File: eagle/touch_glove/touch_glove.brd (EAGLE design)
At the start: 160 x 100 mm, 139 parts, among them P1 PELTIER, P2 PELTIER, P3 PELTIER, P4 PELTIER, P5 PELTIER, U1 DRV8837C, U2 DRV8837C, U3 DRV8837C, U4 DRV8837C, U5 DRV8837C, U6 ATMEGA128RFA1, Y1 16MHz

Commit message: Changed power symbols for Glove
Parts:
- added BATT1: BATTERYPTH_HOLES, MrSwirlyEyes:DUAL_PTH_PADS
- added C63, C64, C65, C66, C69, C70, C71: 10uF/25V, MrSwirlyEyes:CAP_CER_SMD-805
- added C67: 220uF/16V, MrSwirlyEyes:CAP_POL_SMD_L6.6-W6.6
- added C68, C74, C75, C76: 0.1uF/50V, MrSwirlyEyes:CAP_CER_SMD-805
- added C78: 100UF/16V, MrSwirlyEyes:CAP_POL_SMD_L6.6-W6.6
- added C79: 1uF/25V, MrSwirlyEyes:CAP_CER_SMD-805
- added D6, D7, D8: 1A/50V, MrSwirlyEyes:DIODE_SMD_1A-50V-SOD123F
- added L1, L2: 10uH, MrSwirlyEyes:INDUCTOR_SMD-805
- added SW1: 5A/28V, MrSwirlyEyes:SW-SLIDE_SPDT_5A-28V_13L-7W
- added U$1, U$2: NET_BRIDGE, MrSwirlyEyes:NET_BRIDGE
- added VREG1, VREG2: 1.5A/3.3V, MrSwirlyEyes:SOT223-4
- added VREG3: 1.5A/2.5V, MrSwirlyEyes:SOT223-4
- R1, R10, R11, R12, R13, R14, R15, R16, R17, R18, R19, R2, R20, R21, R22, R23, R24, R25, R26, R27, R28, R29, R3, R30, R31, R32, R33, R34, R35, R36, R37, R38, R4, R5, R6, R7, R8, R9: device MrSwirlyEyes:RESC2012X60_HS -> MrSwirlyEyes:RESISTOR_SMD-805
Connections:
- new net 3.3V: C65.1, C70.1, D7.A, D8.A, VREG2.3, VREG3.3
- new net N$38: L2.2, U$2.P$1
- new net N$40: C64.1, C66.1, C67.A, C68.1, C69.1, C71.1, C78.A, D6.K, D7.K, D8.K, SW1.P$1, VREG1.1, VREG2.1, VREG3.1
- new net N$43: BATT1.+, SW1.P$2
- new net NGND: C79.2, U$1.P$1, U$2.P$2
- net GND: now also BATT1.-, C63.2, C64.2, C65.2, C66.2, C67.K, C68.2, C69.2, C70.2, C71.2, C74.2, C78.K, L2.1, U$1.P$2, VREG1.2, VREG1.4, VREG2.2, VREG2.4, VREG3.2, VREG3.4
- net VCC: now also C63.1, C74.1, C79.1, D6.A, L1.1, L1.2, VREG1.3

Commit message: Unity to RED board test added.  Unity to Arduino test moved.  Several changes to Touch Glove sch and brd
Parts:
- removed C76: 0.1uF/50V, MrSwirlyEyes:CAP_CER_SMD-805
- removed D8: 1A/50V, MrSwirlyEyes:DIODE_SMD_1A-50V-SOD123F
- removed VREG1: 1.5A/3.3V, MrSwirlyEyes:SOT223-4
- added C72, C77: 10uF/25V, MrSwirlyEyes:CAP_CER_SMD-805
- added C73, C80: 0.1uF/50V, MrSwirlyEyes:CAP_CER_SMD-805
- added C81: 100UF/16V, MrSwirlyEyes:CAP_POL_SMD_L6.6-W6.6
- added C82: 220uF/16V, MrSwirlyEyes:CAP_POL_SMD_L6.6-W6.6
- added D9: 1A/50V, MrSwirlyEyes:DIODE_SMD_1A-50V-SOD123F
- added VREG4: 3A/2.5V, MrSwirlyEyes:DDPAK-5
- C64, C66, C70: value 10uF/25V -> 0.1uF/50V
- C74: value 0.1uF/50V -> 10uF/25V
- VREG3: value 1.5A/2.5V -> 1A/3.3V; device MrSwirlyEyes:SOT223-4 -> MrSwirlyEyes:SOIC-8_W3.9MM
- moved C71 1313.3 mm to (-345.4, -1162.0)
- moved C70 1305.6 mm to (-335.3, -1162.0)
- moved VREG3 1305.5 mm to (-356.9, -1168.4)
- moved C66 1289.9 mm to (-360.7, -1162.0)
- moved C65 1281.2 mm to (-340.4, -1162.0)
- moved C64 121.8 mm to (-350.5, -1162.0)
- moved C63 108.8 mm to (-330.2, -1162.0)
- moved C74 96.6 mm to (-355.6, -1162.0)
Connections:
- net 3.3V: now also C75.1, C77.1, C80.1, C81.A, C82.A, D9.A, VREG4.4, VREG4.5; no longer C70.1, D8.A, VREG3.3
- net GND: now also C72.2, C73.2, C75.2, C77.2, C80.2, C81.K, C82.K, VREG3.1, VREG4.3, VREG4.TAB; no longer VREG1.2, VREG1.4, VREG3.4
- net N$40: now also C72.1, C73.1, C74.1, D9.K, VREG3.3, VREG3.4, VREG4.1, VREG4.2; no longer D8.K, VREG1.1, VREG3.1
- net VCC: now also C70.1, VREG3.5, VREG3.6; no longer C74.1, VREG1.3

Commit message: Rev 1 of Touch Glove schematic complete.  Putting Touch Glove PCB on hold until Robotic Arm schematic + PCB are done
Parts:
- moved VREG4 1226.4 mm to (68.5, 40.6)
- moved BATT1 1165.6 mm to (-128.3, 102.9)
- moved C62 1165.6 mm to (-138.4, 137.2)
- moved C81 1165.6 mm to (-245.1, 10.2)
- moved JP1 1165.6 mm to (-130.8, 123.2)
- moved SW1 1165.6 mm to (-120.7, 74.9)
- moved U$1 1165.6 mm to (-139.7, 91.4)
- moved VREG3 1165.6 mm to (-283.2, -5.08)
- moved C63 1165.6 mm to (-256.5, 1.27)
- moved C64 1165.6 mm to (-276.9, 1.27)
- moved C65 1165.6 mm to (-266.7, 1.27)
- moved C66 1165.6 mm to (-287.0, 1.27)
- moved C67 1165.6 mm to (-166.4, 52.1)
- moved C68 1165.6 mm to (-182.9, 48.3)
- moved C69 1165.6 mm to (-188.0, 48.3)
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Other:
- board size 160 x 100 mm -> 88.9 x 50.8 mm
- board text removed: "initializing touch_glove"

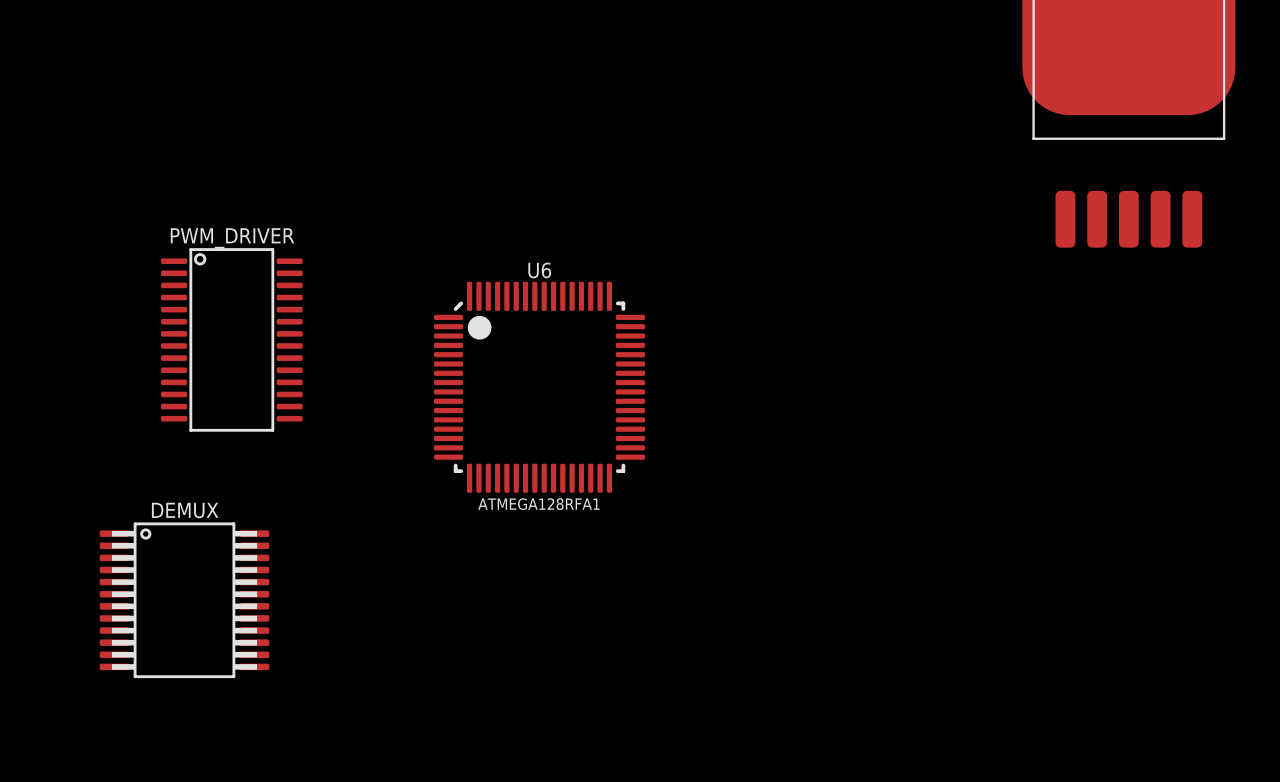
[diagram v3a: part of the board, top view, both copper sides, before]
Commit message: Replaced 2.5V regulator for TECs to 1.8V regulator for TECs.  2.5V got way too hot.  But 1.8V can be used effectively
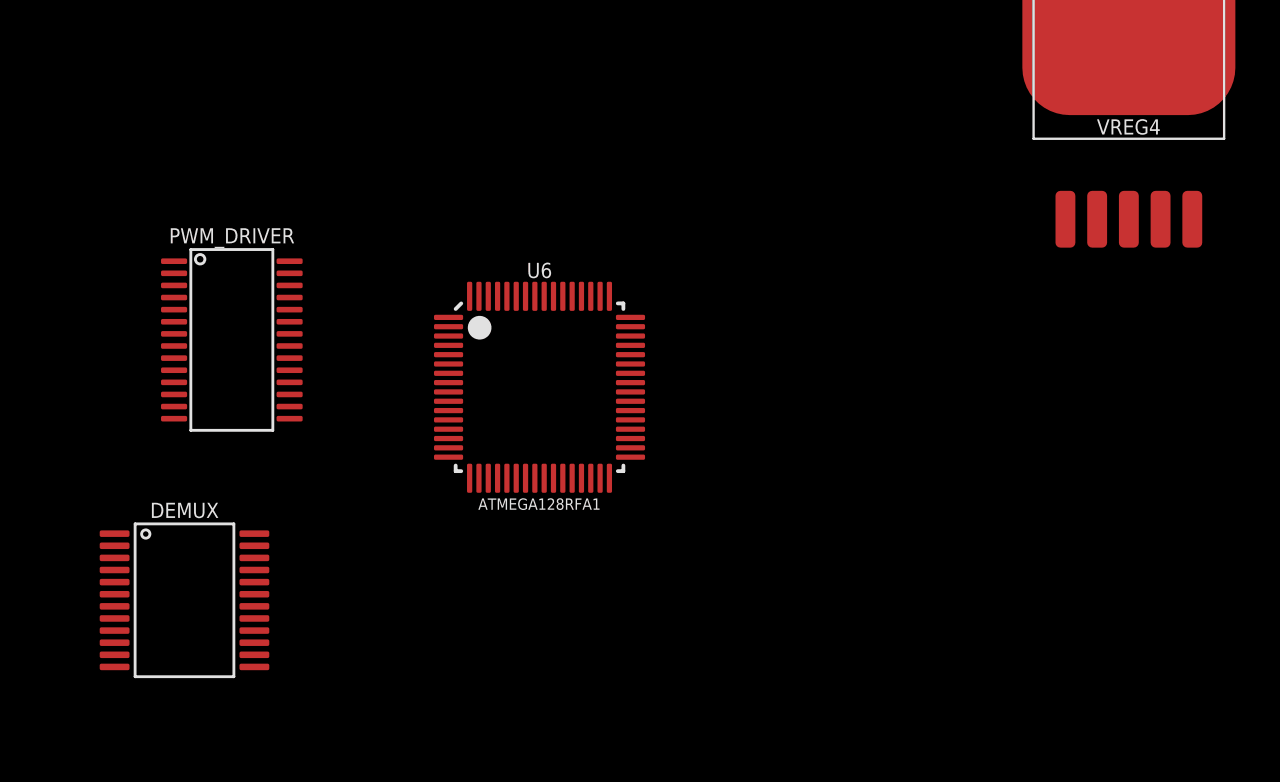
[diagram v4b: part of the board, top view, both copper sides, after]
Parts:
- J1: value (none) -> AVR ISP
- VREG4: value 3A/2.5V -> 3A/1.8V
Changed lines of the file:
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@@
 <attribute name="TESTED" value="NO" x="-173.99" y="-73.66" size="1.778" layer="27" display="off"/>
 </element>
-<element name="J1" library="MrSwirlyEyes" package="2X3-NS" value="" x="-123.19" y="144.78">
+<element name="J1" library="MrSwirlyEyes" package="2X3-NS" value="AVR ISP" x="-123.19" y="144.78">
 <attribute name="DATASHEET" value="http://portal.fciconnect.com/Comergent//fci/drawing/67996.pdf" x="-123.19" y="144.78" size="1.778" layer="27" display="off"/>
 <attribute name="DIST" value="Digikey" x="-123.19" y="144.78" size="1.778" layer="27" display="off"/>
@@
 <attribute name="MFR" value="Amphenol FCI" x="-123.19" y="144.78" size="1.778" layer="27" display="off"/>
 <attribute name="MPN" value="67997-206HLF" x="-123.19" y="144.78" size="1.778" layer="27" display="off"/>
+<attribute name="VALUE" value="AVR ISP" x="-123.19" y="144.78" size="1.778" layer="27" display="off"/>
 </element>
 <element name="C62" library="MrSwirlyEyes" package="CAP_CER_SMD-805" value="0.1uF/50V" x="-138.43" y="137.16">
@@
 <attribute name="TESTED" value="NO" x="-224.79" y="38.1" size="1.778" layer="27" display="off"/>
 </element>
-<element name="VREG4" library="MrSwirlyEyes" package="DDPAK-5" value="3A/2.5V" x="68.453" y="40.64">
+<element name="VREG4" library="MrSwirlyEyes" package="DDPAK-5" value="3A/1.8V" x="68.453" y="40.64">
 <attribute name="CREATOR" value="MrSwirlyEyes" x="68.453" y="40.64" size="1.778" layer="27" display="off"/>
 <attribute name="DATASHEET" value="http://cds.linear.com/docs/en/datasheet/1764fb.pdf" x="68.453" y="40.64" size="1.778" layer="27" display="off"/>
 <attribute name="DIST" value="Digikey" x="68.453" y="40.64" size="1.778" layer="27" display="off"/>
-<attribute name="DISTLINK" value="https://www.digikey.com/products/en?keywords=LT1764EQ-2.5%23PBF-ND" x="68.453" y="40.64" size="1.778" layer="27" display="off"/>
-<attribute name="DISTPN" value="LT1764EQ-2.5#PBF-ND" x="68.453" y="40.64" size="1.778" layer="27" display="off"/>
+<attribute name="DISTLINK" value="https://www.digikey.com/products/en?keywords=LT1764EQ-1.8%23PBF" x="68.453" y="40.64" size="1.778" layer="27" display="off"/>
+<attribute name="DISTPN" value="LT1764EQ-1.8#PBF-ND" x="68.453" y="40.64" size="1.778" layer="27" display="off"/>
 <attribute name="MFR" value="Linear Technology" x="68.453" y="40.64" size="1.778" layer="27" display="off"/>
-<attribute name="MPN" value="LT1764EQ-2.5#PBF" x="68.453" y="40.64" size="1.778" layer="27" display="off"/>
+<attribute name="MPN" value="LT1764EQ-1.8#PBF" x="68.453" y="40.64" size="1.778" layer="27" display="off"/>
 </element>
 <element name="C72" library="MrSwirlyEyes" package="CAP_CER_SMD-805" value="10uF/25V" x="-229.87" y="17.78">

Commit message: Modified code to work with new PCB board.  Removed libraries, placed in new repo.  Finished and printed Robotic Arm PCB board.  Tested and WORKS!  Started on Touch Glove PCB
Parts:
- removed A1: ANTENNASMD5, lib_kenmei:ANTENNA-CHIP5
- removed B1: 748421245, lib_kenmei:0805_BALUN
- removed C36, C38, C40, C41, C47: 1uF/25V, MrSwirlyEyes:CAP_CER_SMD-805
- removed C37, C39, C46, C51, C62: 0.1uF/50V, MrSwirlyEyes:CAP_CER_SMD-805
- removed C42, C43: 12pF/250V, MrSwirlyEyes:CAP_CER_SMD-805
- removed C44: 22PF/250V, MrSwirlyEyes:CAP_CER_SMD-805
- removed C45: 0.75PF/100V, MrSwirlyEyes:CAP_CER_SMD-805
- removed C48: 0.22uF/50V, MrSwirlyEyes:CAP_CER_SMD-805
- removed C49, C50: 10uF/25V, MrSwirlyEyes:CAP_CER_SMD-805
- removed DEMUX: CH16_MUX-DEMUX, MrSwirlyEyes:SSOP-24
- removed IMU1: LM9DS1, lib_kenmei:LSM9DS1_LGA24L
- removed J1: AVR ISP, MrSwirlyEyes:2X3-NS
- removed JP1: FTDIPTH-RA, MrSwirlyEyes:FTDI_BASIC-6PIN-MALE-RA
- removed R38: 10KΩ, MrSwirlyEyes:RESISTOR_SMD-805
- removed U6: ATMEGA128RFA1, MrSwirlyEyes:VFQFN-64
- removed Y1: 16MHz, MrSwirlyEyes:CRYSTAL-SMD-5X3
- added A6: 2.4GHz/802.11/0.5dBi/3W, PiB_radio_frequency:ANTENNA-CHIP5
- added ANALOG_BR, NOISE_BR: 2PT_GND_TIE, PiB_power_symbols:2PT_GND_TIE
- added AVR_ISP: AVR ISP, PiB_connectors:2X3-NS
- added B2: Impedence UNBAL/BAL (50Ω/100Ω), PiB_radio_frequency:0805_BALUN
- added BATT2: BATTERYPTH_HOLES, PiB:DUAL_PTH_PADS
- added C100, C106, C108, C116, C117, C119, C121, C122, C124, C127, C129, C135, C98: 0.1uF/50V, PiB_capacitors:_CER_SMD-805
- added C107, C109, C110, C111, C132, C134, C136: 1uF/25V, PiB_capacitors:_CER_SMD-805
- added C112, C113: 12pF/250V, PiB_capacitors:_CER_SMD-805
- added C114: 22PF/250V, PiB_capacitors:_CER_SMD-805
- added C115: 0.75PF/100V, PiB_capacitors:_CER_SMD-805
- added C118: 220uF/16V, PiB_capacitors:_AE_SMD_L6.6-W6.6
- added C120, C123, C125, C126, C128, C97, C99: 10uF/25V, PiB_capacitors:_CER_SMD-805
- added C133: 100UF/16V, PiB_capacitors:_AE_SMD_L6.6-W6.6
- added D10, D11, D8: 1A/50V, PiB_discrete_semiconductors:SOD123F
- added D12: 1A/50V, MrSwirlyEyes:DIODE_SMD_1A-50V-SOD123F
- added DEMUX1: CH16_MUX-DEMUX, PiB:SSOP-24
- added J2: (ID,OD)=(2.1,5.5)MM, PiB_connectors:POWER_JACK_SLOT_ID2.1MM-OD5.5MM
- added JP2: FTDIPTH-RA, PiB_connectors:FTDI_BASIC-6PIN-MALE-RA
- added L3, L4: 10uH, PiB_inductors:_SMD-805
- added L5: BLUE, PiB_leds:LED_SMD-805_
- added L6: GREEN, PiB_leds:LED_SMD-805_
- added L7: RED, PiB_leds:LED_SMD-805_
- added MCU: ATMEGA128RFA1, PiB_ic_microcontrollers:VFQFN-64
- added PWM_DRIVER1: PCA9685, PiB:TSSOP-28
- added R40, R41: 4.7K, PiB_resistors:RESISTOR_SMD-805
- added R46, R47: 10KΩ, PiB_resistors:RESISTOR_SMD-805
- added R48: 2KΩ, PiB_resistors:RESISTOR_SMD-805
- added R49: 1KΩ, PiB_resistors:RESISTOR_SMD-805
- added S7: TACTILE-SW_500mA/12V, PiB_switches:BTN_MOMENTARY_SPST-NO_SMD_12V_50MA_L5.2-W5.2
- added SW2: 5A/28V, PiB_switches:SW_TOGGLE_SPDT_5A-28V_13L-7W
- added VIBE_6: VIBE_MOTOR, MrSwirlyEyes:CONNECTOR_VIBE-MOTOR
- added VIBE_T6: 2.6A/20V/57mΩ, MrSwirlyEyes:SOT23-3
- added VREG1: 1A/3.3V, PiB_ic_power:SOIC-8_W3.9MM
- added VREG5: 5A/5V, PiB_ic_power:TO-263-5
- added Y2: 16MHz, PiB:CRYSTAL-SMD-5X3
- C1: value 10uF/25V -> 0.1uF/50V
- C35: value 0.1uF/50V -> 10uF/25V
- R12: value 4.7K -> 10KΩ
- R13: value 4.7K -> 100Ω
- moved R12 399.9 mm to (-276.9, -266.7)
- moved R13 395.9 mm to (-271.8, -266.7)
- moved C24 393.5 mm to (-287.0, -266.7)
- moved C1 357.5 mm to (-266.7, -259.1)
- moved C35 331.6 mm to (-281.9, -266.7)
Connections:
- removed net C5: DEMUX.4
- removed net C6: DEMUX.3
- removed net C7: DEMUX.2
- removed net C8: DEMUX.23
- removed net C9: DEMUX.22
- removed net N$33: B1.4, U6.8
- removed net N$34: B1.2, C44.1
- removed net N$35: C42.1, U6.56, Y1.1
- removed net N$36: C49.1, IMU1.21
- removed net N$37: C48.1, IMU1.24
- removed net N$39: A1.FEED, B1.1, C45.1
- removed net N$41: C62.1, JP1.DTR
- removed net N$42: JP1.CTS
- removed net S0: DEMUX.10
- removed net S1: DEMUX.11
- removed net S2: DEMUX.14
- removed net S3: DEMUX.13
- removed net SIG: DEMUX.1
- new net 5V: C121.1, C125.1, C133.A, D10.A, VREG5.4
- new net AGND: ANALOG_BR.P$2, C100.2, C122.2, C134.2, C135.2, C136.2, C97.2, DEMUX1.12, DEMUX1.15, MCU.58, MCU.61
- new net AVCC: C100.1, C122.1, C134.1, C135.1, C136.1, C97.1, DEMUX1.24, L3.2, MCU.59, MCU.62
- new net BATT_+: BATT2.+, J2.PWR, SW2.2
- new net BATT_-: BATT2.-, J2.GND@2
- new net N$44: C113.1, MCU.57, Y2.3
- new net N$45: B2.3, MCU.9
- new net N$46: B2.4, MCU.8
- new net N$47: B2.2, C114.1
- new net N$48: C112.1, MCU.56, Y2.1
- new net N$49: A6.FEED, B2.1, C115.1
- new net N$50: C117.1, JP2.DTR
- new net N$51: JP2.CTS
- new net N$52: ANALOG_BR.P$1, L4.2
- new net N$53: L5.K, R47.2
- new net N$54: L6.K, R49.2
- new net N$55: L7.K, R48.2
- new net N$62: C132.1, MCU.21, MCU.22
- new net N$63: C110.1, MCU.60
- new net STRAIN_10: DEMUX1.22
- new net STRAIN_6: DEMUX1.4
- new net STRAIN_7: DEMUX1.3
- new net STRAIN_8: DEMUX1.2
- new net STRAIN_9: DEMUX1.23
- new net VBATT: C118.A, C119.1, C120.1, C126.1, C127.1, C128.1, C129.1, D10.K, D8.K, L5.A, SW2.1, VREG1.3, VREG1.4, VREG5.1, VREG5.2
- new net VIBE_6: PWM_DRIVER.22, R12.2, R13.1
- net A0: now also MCU.63; no longer U6.63
- net A1: now also MCU.64; no longer U6.64
- net A2: now also MCU.1; no longer U6.1
- net A3: now also MCU.2; no longer U6.2
- net A4: now also MCU.3; no longer U6.3
- net A5: now also DEMUX1.1, MCU.4; no longer U6.4
- net A6: now also MCU.5; no longer U6.5
- net A7: now also MCU.6; no longer U6.6
- net C10: now also DEMUX1.21; no longer DEMUX.21
- net C11: now also DEMUX1.20; no longer DEMUX.20
- net C12: now also DEMUX1.19; no longer DEMUX.19
- net C13: now also DEMUX1.18; no longer DEMUX.18
- net C14: now also DEMUX1.17; no longer DEMUX.17
- net C15: now also DEMUX1.16; no longer DEMUX.16
- net GND: now also AVR_ISP.6, B2.5, C106.2, C107.2, C108.2, C109.2, C110.2, C111.2, C112.2, C113.2, C114.2, C115.2, C116.2, C118.K, C119.2, C120.2, C123.2, C124.2, C126.2, C127.2, C132.2, C98.2, C99.2, J2.GND@1, JP2.GND, L4.1, MCU.10, MCU.11, MCU.20, MCU.24, MCU.33, MCU.35, MCU.45, MCU.55, MCU.7, NOISE_BR.P$2, PWM_DRIVER1.1, PWM_DRIVER1.14, PWM_DRIVER1.2, PWM_DRIVER1.23, PWM_DRIVER1.24, PWM_DRIVER1.25, PWM_DRIVER1.3, PWM_DRIVER1.4, PWM_DRIVER1.5, R12.1, R47.1, R48.1, R49.1, S7.1, VIBE_T6.S, VREG1.1, VREG1.2; no longer B1.5, C1.2, C36.2, C37.2, C38.2, C39.2, C40.2, C41.2, C42.2, C43.2, C44.2, C45.2, C46.2, C47.2, C48.2, C49.2, C50.2, C51.2, DEMUX.12, DEMUX.15, IMU1.14, IMU1.15, IMU1.16, IMU1.17, IMU1.18, IMU1.19, IMU1.20, J1.6, JP1.GND, U6.10, U6.11, U6.20, U6.24, U6.33, U6.35, U6.45, U6.55, U6.58, U6.61, U6.7
- net MISO: now also AVR_ISP.1, MCU.39; no longer J1.1, U6.39
- net MOSI: now also AVR_ISP.4, MCU.38; no longer J1.4, U6.38
- net N$30: now also C1.2, D12.A, VIBE_6.2, VIBE_T6.D; no longer C43.1, U6.57, Y1.3
- net N$32: now also R13.2, VIBE_T6.G; no longer B1.3, U6.9
- net NGND: now also C121.2, C125.2, C128.2, C129.2, C133.K, NOISE_BR.P$1, VREG5.3, VREG5.TAB
- net PB4: now also MCU.40; no longer U6.40
- net PB5: now also MCU.41; no longer U6.41
- net PB6: now also L7.A, MCU.42; no longer U6.42
- net PB7: now also L6.A, MCU.43; no longer U6.43
- net PD4: now also MCU.29; no longer U6.29
- net PD5: now also MCU.30; no longer U6.30
- net PD6: now also MCU.31; no longer U6.31
- net PD7: now also MCU.32; no longer U6.32
- net PE2: now also DEMUX1.10, MCU.48; no longer U6.48
- net PE3: now also MCU.49; no longer U6.49
- net PE4: now also MCU.50; no longer U6.50
- net PE5: now also MCU.51; no longer U6.51
- net PE6: now also DEMUX1.11, MCU.52; no longer U6.52
- net PE7: now also DEMUX1.14, MCU.53; no longer U6.53
- net PG0: now also MCU.14; no longer U6.14
- net PG1: now also MCU.15; no longer U6.15
- net PG2: now also MCU.16; no longer U6.16
- net PG3: now also MCU.17; no longer U6.17
- net PG4: now also MCU.18; no longer U6.18
- net PG5: now also MCU.19; no longer U6.19
- net PWM10: now also PWM_DRIVER1.17; no longer PWM_DRIVER.17
- net RESET: now also AVR_ISP.5, C117.2, D11.A, MCU.12, R46.1, S7.3; no longer C62.2, J1.5, R38.1, U6.12
- net RX0: now also JP2.TXO, MCU.46; no longer JP1.TXO, U6.46
- net RX1: now also MCU.27; no longer U6.27
- net SCK: now also AVR_ISP.3, MCU.37; no longer J1.3, U6.37
- net SCL: now also MCU.25, PWM_DRIVER1.26, R40.1; no longer IMU1.2, R12.1, U6.25
- net SDA: now also MCU.26, PWM_DRIVER1.27, R41.1; no longer IMU1.4, R13.1, U6.26
- net SSN: now also DEMUX1.13, MCU.36; no longer U6.36
- net STRAIN_1: now also DEMUX1.9; no longer DEMUX.9
- net STRAIN_2: now also DEMUX1.8; no longer DEMUX.8
- net STRAIN_3: now also DEMUX1.7; no longer DEMUX.7
- net STRAIN_4: now also DEMUX1.6; no longer DEMUX.6
- net STRAIN_5: now also DEMUX1.5; no longer DEMUX.5
- net TEC_1_COLD: now also PWM_DRIVER1.7
- net TEC_1_HOT: now also PWM_DRIVER1.6
- net TEC_2_COLD: now also PWM_DRIVER1.9
- net TEC_2_HOT: now also PWM_DRIVER1.8
- net TEC_3_COLD: now also PWM_DRIVER1.11
- net TEC_3_HOT: now also PWM_DRIVER1.10
- net TEC_4_COLD: now also PWM_DRIVER1.13
- net TEC_4_HOT: now also PWM_DRIVER1.12
- net TEC_5_COLD: now also PWM_DRIVER1.16
- net TEC_5_HOT: now also PWM_DRIVER1.15
- net TX0: now also JP2.RXI, MCU.47; no longer JP1.RXI, U6.47
- net TX1: now also MCU.28; no longer U6.28
- net VCC: now also AVR_ISP.2, C106.1, C107.1, C108.1, C109.1, C111.1, C116.1, C123.1, C124.1, C98.1, C99.1, D11.K, D12.K, D8.A, JP2.VCC, L3.1, MCU.23, MCU.34, MCU.44, MCU.54, PWM_DRIVER1.28, R40.2, R41.2, R46.2, VIBE_6.1, VREG1.5, VREG1.6; no longer C36.1, C37.1, C38.1, C39.1, C40.1, C41.1, C46.1, C47.1, C50.1, C51.1, DEMUX.24, IMU1.1, IMU1.22, IMU1.23, IMU1.3, J1.2, JP1.VCC, R12.2, R13.2, R38.2, U6.21, U6.22, U6.23, U6.34, U6.44, U6.54, U6.59, U6.60, U6.62
- net VIBE_1: now also PWM_DRIVER.17, PWM_DRIVER1.18; no longer PWM_DRIVER.18
- net VIBE_2: now also PWM_DRIVER.18, PWM_DRIVER1.19; no longer PWM_DRIVER.19
- net VIBE_3: now also PWM_DRIVER.19, PWM_DRIVER1.20; no longer PWM_DRIVER.20
- net VIBE_4: now also PWM_DRIVER.20, PWM_DRIVER1.21; no longer PWM_DRIVER.21
- net VIBE_5: now also PWM_DRIVER.21, PWM_DRIVER1.22; no longer PWM_DRIVER.22
